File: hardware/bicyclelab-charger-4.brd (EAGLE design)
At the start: 87 x 27.9 mm, 45 parts, among them IC1 LDO-5V-0.5A, IC2 TINY24/44/84-SSU, Q1 BC817-16SMD, Q2 FDP5800

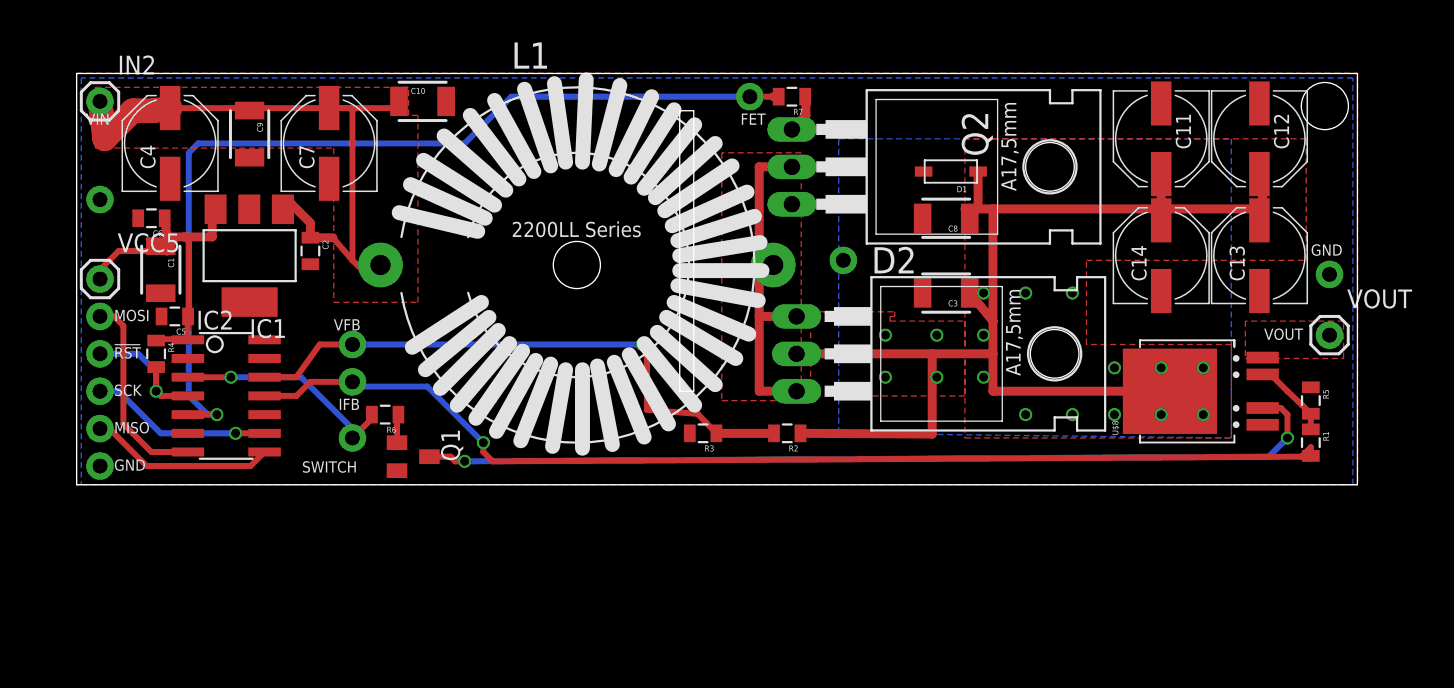
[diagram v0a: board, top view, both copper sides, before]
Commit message: clean refactoring of latest tested implementation
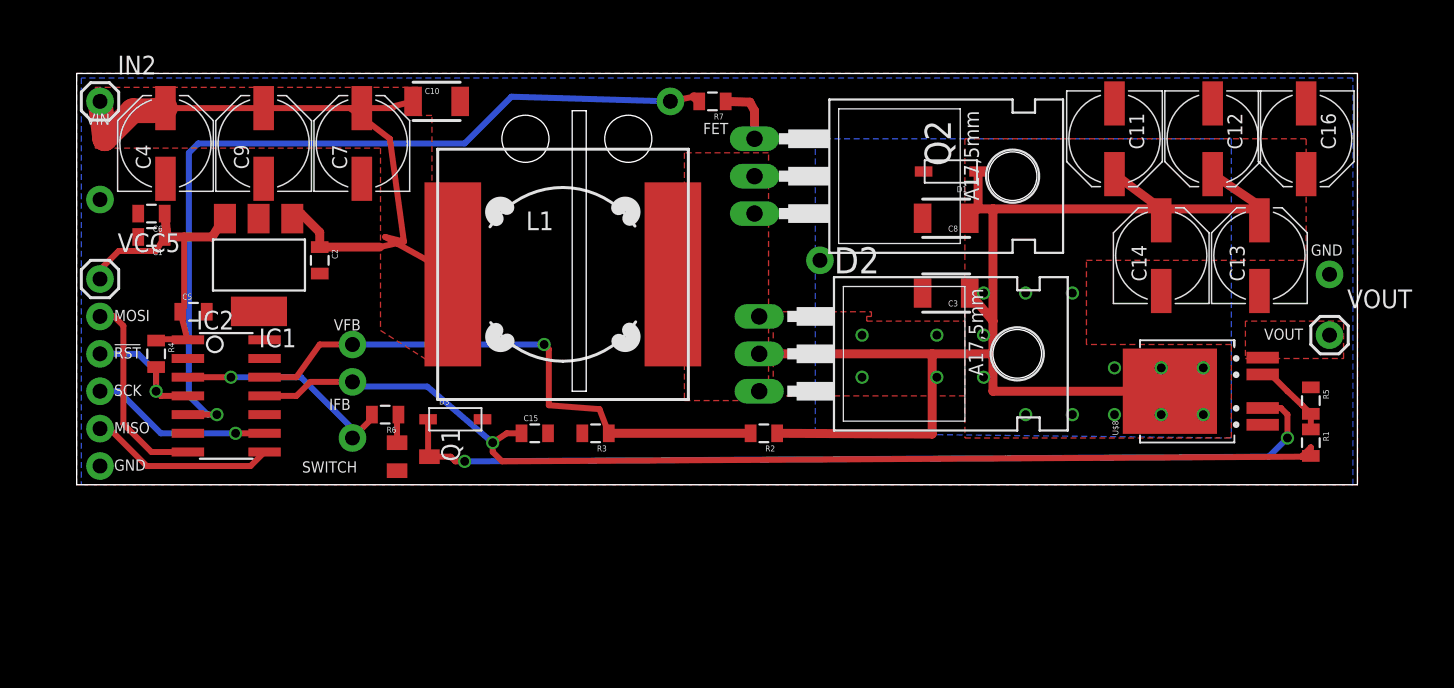
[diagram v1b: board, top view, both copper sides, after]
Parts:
- added C15: 1uF, SparkFun:0805
- added C16: 100uF, adafruit:PANASONIC_D
- added D3: (no value), adafruit:SOD-123
- C1: device bicyclelab:1210 -> bicyclelab:0805
- C9: value 10uF -> 100uF; device bicyclelab:1210 -> adafruit:PANASONIC_D
- L1: device bicyclelab:2200LL -> bicyclelab:DR175
- moved R3 7.30 mm to (35.2, 3.49)
- moved FET 5.41 mm to (40.3, 26.0)
- moved R7 5.41 mm to (43.2, 26.0)
- moved C11 3.17 mm to (70.5, 23.5)
- moved C12 3.17 mm to (77.2, 23.5)
- moved Q2 2.62 mm to (52.4, 21.0)
- moved D2 2.54 mm to (52.7, 8.89)
- moved C1 2.31 mm to (5.08, 16.8), turned to 180 degrees
- moved C7 2.22 mm to (19.4, 23.2)
- moved R2 1.59 mm to (46.7, 3.49)
- moved VBOOST 1.59 mm to (50.5, 15.2)
- moved C5 1.31 mm to (7.94, 11.7), turned to 0 degrees
- moved C9 1.14 mm to (12.7, 23.2), turned to 90 degrees
- moved L1 1.14 mm to (33.0, 14.3)
- moved C10 0.95 mm to (24.4, 26.0)
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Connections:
- net GND: now also C15.2, C16.-, C9.-, D3.A; no longer C9.2
- net IFB: now also C15.1
- net N$10: now also D3.C
- net VBOOST: now also C16.+
- net VIN: now also C9.+; no longer C9.1
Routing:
- net VFET: track 23.5 -> 0.00 mm
- net VBOOST: track 83.8 -> 91.4 mm
- net VIN: track 45.9 -> 51.5 mm
- net N$1: track 62.5 -> 57.3 mm
- net N$10: track 62.4 -> 65.0 mm
- net IFB: track 74.9 -> 76.9 mm
- net N$4: track 2.64 -> 4.21 mm
- net VFB: track 40.6 -> 39.2 mm
- net VCC: track 22.5 -> 22.0 mm
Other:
- outline, holes or cut-outs redrawn

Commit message: refactor charger code
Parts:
- added R8: 10k, SparkFun:0805
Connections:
- net GND: now also R8.2
- net SWITCH: now also R8.1
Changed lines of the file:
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@@
 <element name="C15" library="SparkFun" package="0805" value="1uF" x="31.115" y="3.4925"/>
 <element name="C16" library="adafruit" package="PANASONIC_D" value="100uF" x="83.5025" y="23.495" rot="R270"/>
+<element name="R8" library="SparkFun" package="0805" value="10k" x="-1.905" y="-11.1125"/>
 </elements>
 <signals>
@@
 <contactref element="C15" pad="2"/>
 <contactref element="C16" pad="-"/>
+<contactref element="R8" pad="2"/>
+<wire x1="77.1525" y1="25.895" x2="83.5025" y2="25.895" width="0" layer="19" extent="1-1"/>
+<wire x1="70.485" y1="25.895" x2="77.1525" y2="25.895" width="0" layer="19" extent="1-1"/>
+<wire x1="85.09" y1="14.2875" x2="83.5025" y2="25.895" width="0" layer="19" extent="1-1"/>
+<wire x1="80.3275" y1="13.1575" x2="85.09" y2="14.2875" width="0" layer="19" extent="1-1"/>
+<wire x1="73.66" y1="13.1575" x2="80.3275" y2="13.1575" width="0" layer="19" extent="1-1"/>
+<wire x1="83.82" y1="6.615" x2="80.3275" y2="13.1575" width="0" layer="19" extent="1-1"/>
+<wire x1="57.5225" y1="21.2725" x2="70.485" y2="25.895" width="0" layer="19" extent="1-1"/>
+<wire x1="57.455" y1="18.0975" x2="57.5225" y2="21.2725" width="0" layer="19" extent="1-1"/>
+<wire x1="57.455" y1="13.0175" x2="57.455" y2="18.0975" width="0" layer="19" extent="1-1"/>
+<wire x1="46.0375" y1="18.415" x2="57.455" y2="18.0975" width="0" layer="19" extent="1-1"/>
+<wire x1="34.3425" y1="3.4925" x2="46.0375" y2="18.415" width="0" layer="19" extent="1-1"/>
+<wire x1="32.015" y1="3.4925" x2="34.3425" y2="3.4925" width="0" layer="19" extent="1-1"/>
+<wire x1="27.5675" y1="4.445" x2="32.015" y2="3.4925" width="0" layer="19" extent="1-1"/>
+<wire x1="21.76" y1="0.955" x2="27.5675" y2="4.445" width="0" layer="19" extent="1-1"/>
+<wire x1="12.7635" y1="9.8425" x2="21.76" y2="0.955" width="0" layer="19" extent="1-1"/>
+<wire x1="8.8375" y1="11.7475" x2="12.7635" y2="9.8425" width="0" layer="19" extent="1-1"/>
+<wire x1="16.51" y1="14.34" x2="12.7635" y2="9.8425" width="0" layer="19" extent="1-1"/>
+<wire x1="12.3571" y1="18.0721" x2="16.51" y2="14.34" width="0" layer="19" extent="1-1"/>
+<wire x1="12.7" y1="20.7775" x2="12.3571" y2="18.0721" width="0" layer="19" extent="1-1"/>
+<wire x1="19.3675" y1="20.7775" x2="12.7" y2="20.7775" width="0" layer="19" extent="1-1"/>
+<wire x1="6.0325" y1="20.7775" x2="12.7" y2="20.7775" width="0" layer="19" extent="1-1"/>
+<wire x1="4.18" y1="18.415" x2="6.0325" y2="20.7775" width="0" layer="19" extent="1-1"/>
+<wire x1="4.18" y1="16.8275" x2="4.18" y2="18.415" width="0" layer="19" extent="1-1"/>
+<wire x1="1.5875" y1="19.3675" x2="4.18" y2="18.415" width="0" layer="19" extent="1-1"/>
+<wire x1="26.0475" y1="26.035" x2="19.3675" y2="20.7775" width="0" layer="19" extent="1-1"/>
+<wire x1="1.5875" y1="1.27" x2="8.8375" y2="11.7475" width="0" layer="19" extent="1-1"/>
+<wire x1="-1.005" y1="-11.1125" x2="1.5875" y2="1.27" width="0" layer="19" extent="1-1"/>
 </signal>
 <signal name="VBOOST">
@@
 <wire x1="20.055" y1="4.7625" x2="20.055" y2="4.4975" width="0.4064" layer="1"/>
 <wire x1="20.055" y1="4.4975" x2="18.7325" y2="3.175" width="0.4064" layer="1"/>
+<contactref element="R8" pad="1"/>
+<wire x1="7.5565" y1="7.3025" x2="-2.805" y2="-11.1125" width="0" layer="19" extent="1-1"/>
 </signal>
 <signal name="IFB">

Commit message: prototype is working now. did some adjustement as fine tunning
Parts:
- added D4: DIODE-SCHOTTKYSOD128, bicyclelab:SOD-128
- R5: value 5k6 -> 10k
- moved R8 22.8 mm to (15.9, 3.17), turned to 180 degrees
- moved R2 6.67 mm to (40.0, 3.49)
- moved C2 3.17 mm to (18.4, 17.8), turned to 0 degrees
- moved GND 2.86 mm to (85.1, 17.1)
- moved VOUT 2.86 mm to (85.1, 13.0)
- moved C15 1.91 mm to (33.0, 3.49)
- moved D3 1.59 mm to (27.0, 3.49)
- moved R3 1.59 mm to (36.8, 3.49)
- moved C1 0.32 mm to (5.08, 16.5)
- moved C6 0.32 mm to (5.08, 18.1)
- moved VFB 0.32 mm to (18.7, 9.84)
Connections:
- new net N$8: D4.1, VOUT.1
- net VOUT: now also D4.2; no longer VOUT.1
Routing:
- net VBOOST: track 91.4 -> 98.0 mm
- net VFB: track 39.2 -> 33.2 mm
- net N$8: track 0.00 -> 3.18 mm
- net IFB: track 76.9 -> 79.4 mm
- net SWITCH: track 15.8 -> 17.8 mm
- net N$10: track 65.0 -> 64.5 mm
